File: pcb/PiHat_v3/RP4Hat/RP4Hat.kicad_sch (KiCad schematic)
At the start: 13 parts, among them J5 Conn_01x02, J6 Raspberry_Pi_4, U2 AP2112K-3.3

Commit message: reorganize schematic into subsheets
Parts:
- added C16: 1uF, Capacitor_SMD:C_0805_2012Metric_Pad1.18x1.45mm_HandSolder, symbol Device:C
- added C17: 22uF, Capacitor_SMD:C_1206_3216Metric_Pad1.33x1.80mm_HandSolder, symbol Device:C
- added J11: Conn_01x02, Connector_JST:JST_PH_S2B-PH-K_1x02_P2.00mm_Horizontal, symbol Connector_Generic:Conn_01x02
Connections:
- net +5V: now also C16.1, C17.1, J11.1 (Pin_1)
- net GND: now also C16.2, C17.2, J11.2 (Pin_2)
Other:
- sheet VexBrainPort ports: added A, B, EN, RSRX, RSTX; removed none
- note added: "Communication from PI -> VEX BRAIN"
- note added: "Linear Regulator (5V -> 3.3 V)"
- note added: "Power Supply for +5V fan (OUT)"
- note added: "Power Supply for PI hat (IN)"
- note added: "Tracking Wheel Ports (IN)"
- note removed: "Linear Regulator"
- note removed: "Power Supply"
- note removed: "Tracking Wheel Ports"
- moved on the sheet: C20, C4, U2

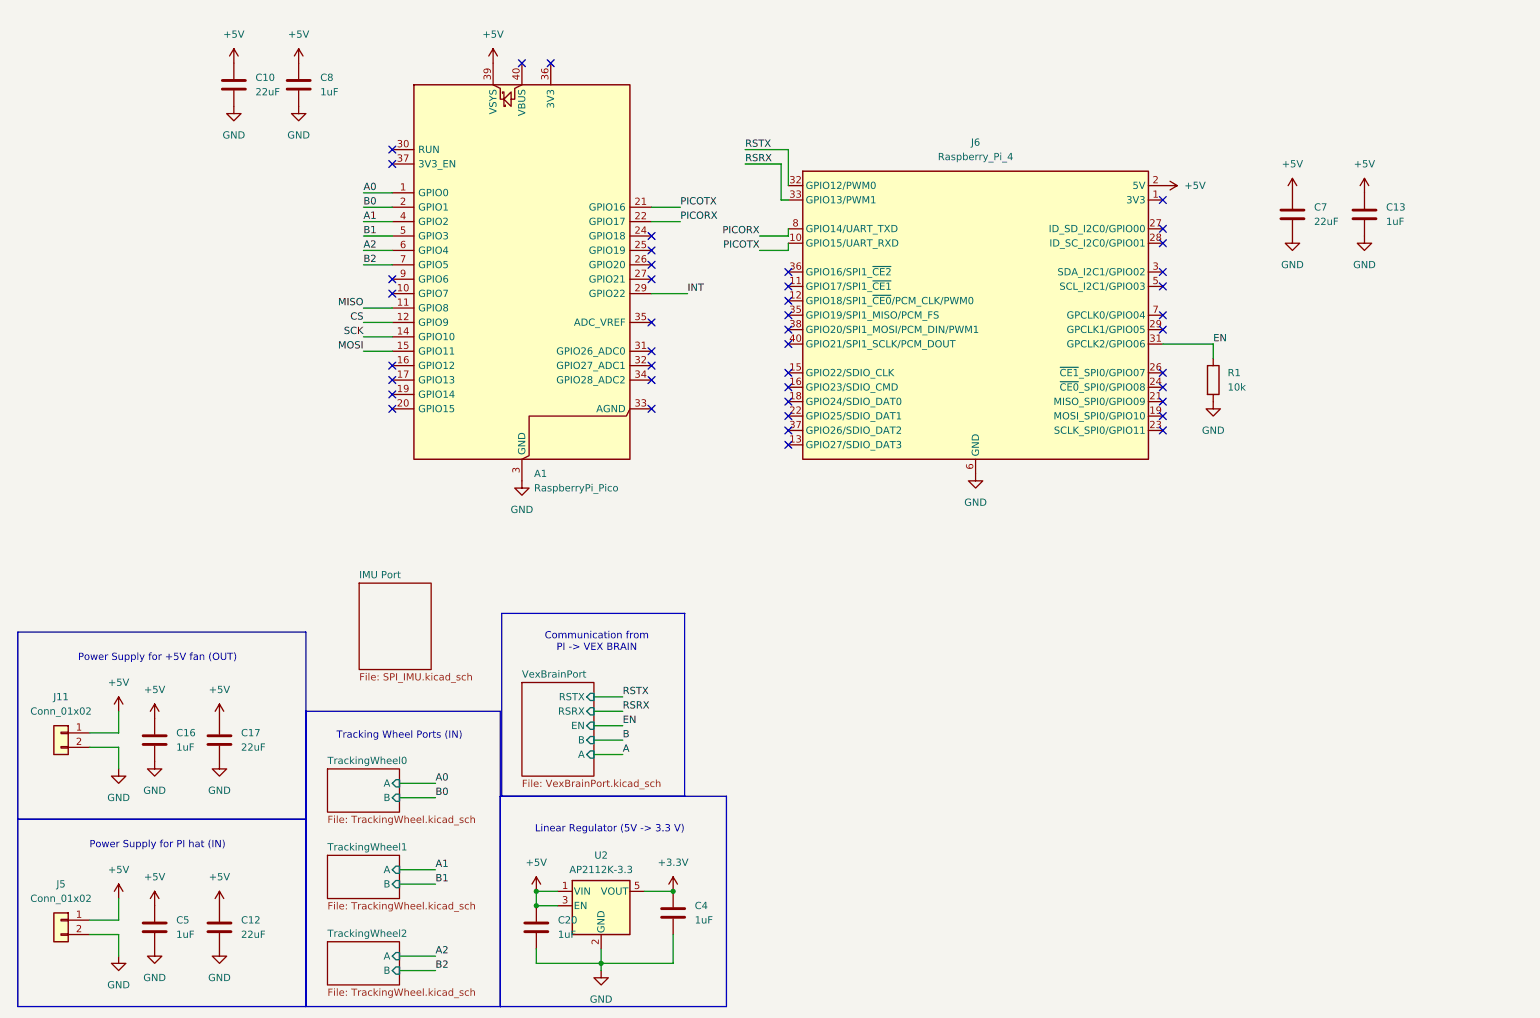
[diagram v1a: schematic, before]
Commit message: move pulldown resistor into sheet
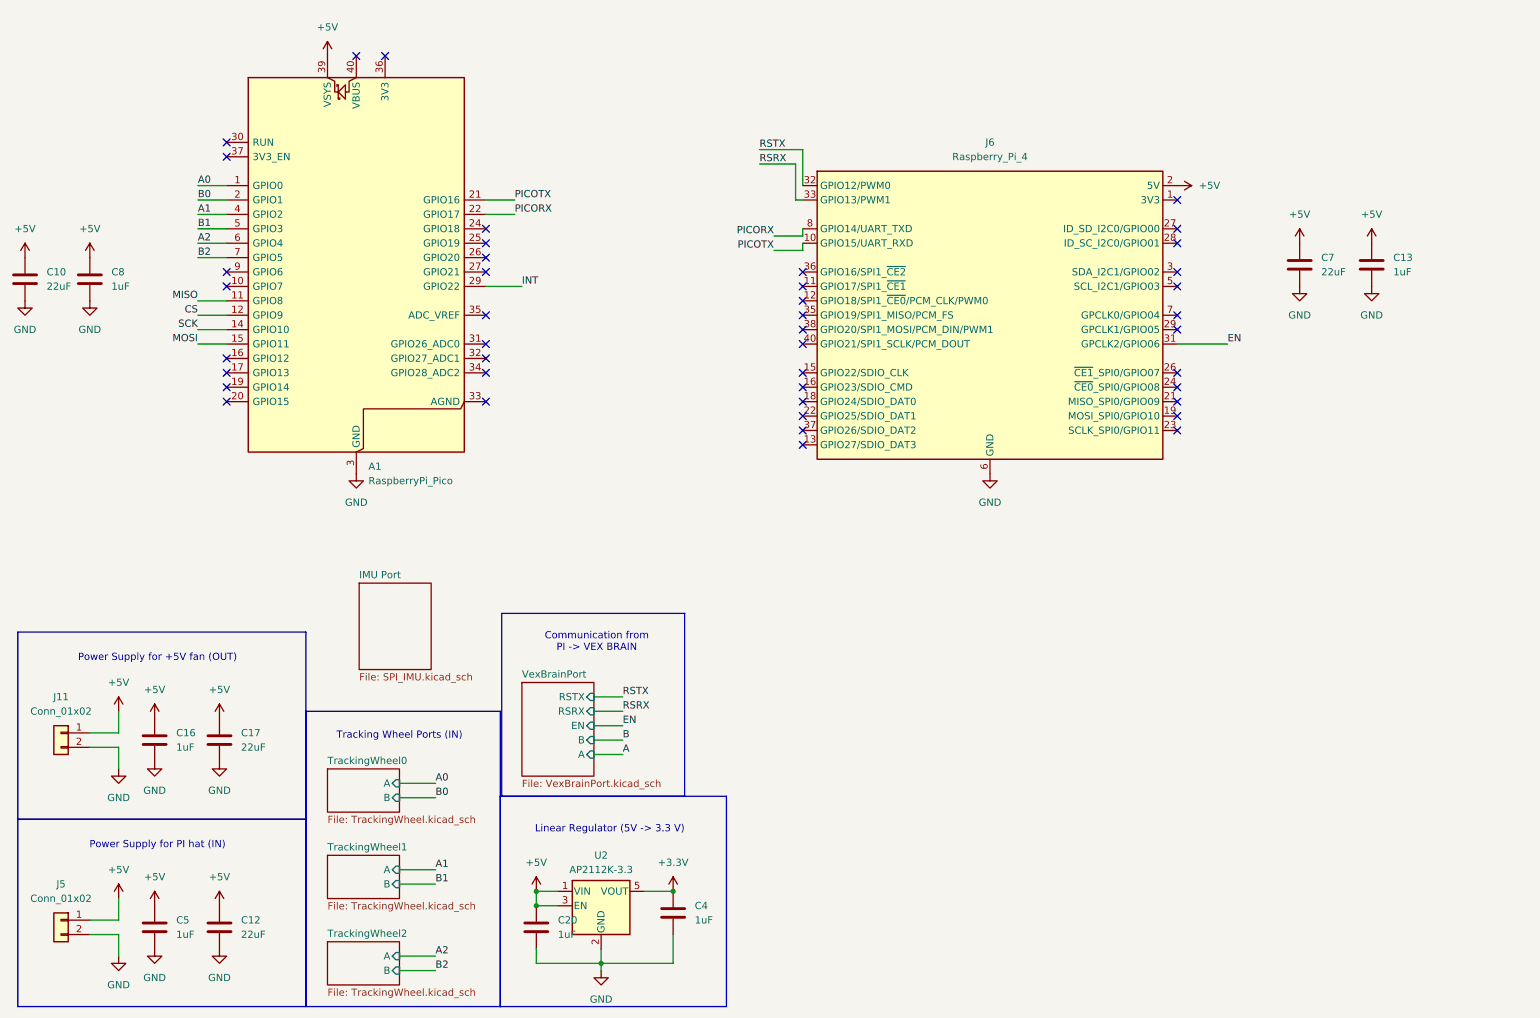
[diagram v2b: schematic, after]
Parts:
- removed R1: 10k, Resistor_SMD:R_0805_2012Metric_Pad1.20x1.40mm_HandSolder, symbol Device:R
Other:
- moved on the sheet: A1, C10, C13, C7, C8, J6

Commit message: organize schematic further, no functional changes
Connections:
- net A0 renamed TW0_A
- net A1 renamed TW1_A
- net A2 renamed TW2_A
- net B0 renamed TW0_B
- net B1 renamed TW1_B
- net B2 renamed TW2_B
- net CS renamed IMU0_CS
- net INT: no longer names the net of A1.29 (GPIO22)
- net MISO renamed IMU0_MISO
- net MOSI renamed IMU0_MOSI
- net SCK renamed IMU0_SCK
- no-connect marks 43 -> 44
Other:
- sheet IMU Port ports: added CS, MISO, MOSI, SCK; removed none
- note added: "Decoupling Caps"
- note added: "Raspberry Pi 4 Model B connections (40 pin header)"
- note added: "Raspberry Pi Pico Connections (PICO soldered onto board)"
- moved on the sheet: A1, C10, C13, C7, C8, J6

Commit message: big potato shi
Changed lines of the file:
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@@
 		)
 	)
-	(label "TW_B"
+	(label "TW2_B"
 		(at 92.71 181.61 0)
 		(effects
